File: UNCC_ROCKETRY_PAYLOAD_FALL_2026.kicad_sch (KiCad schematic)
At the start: 0 parts

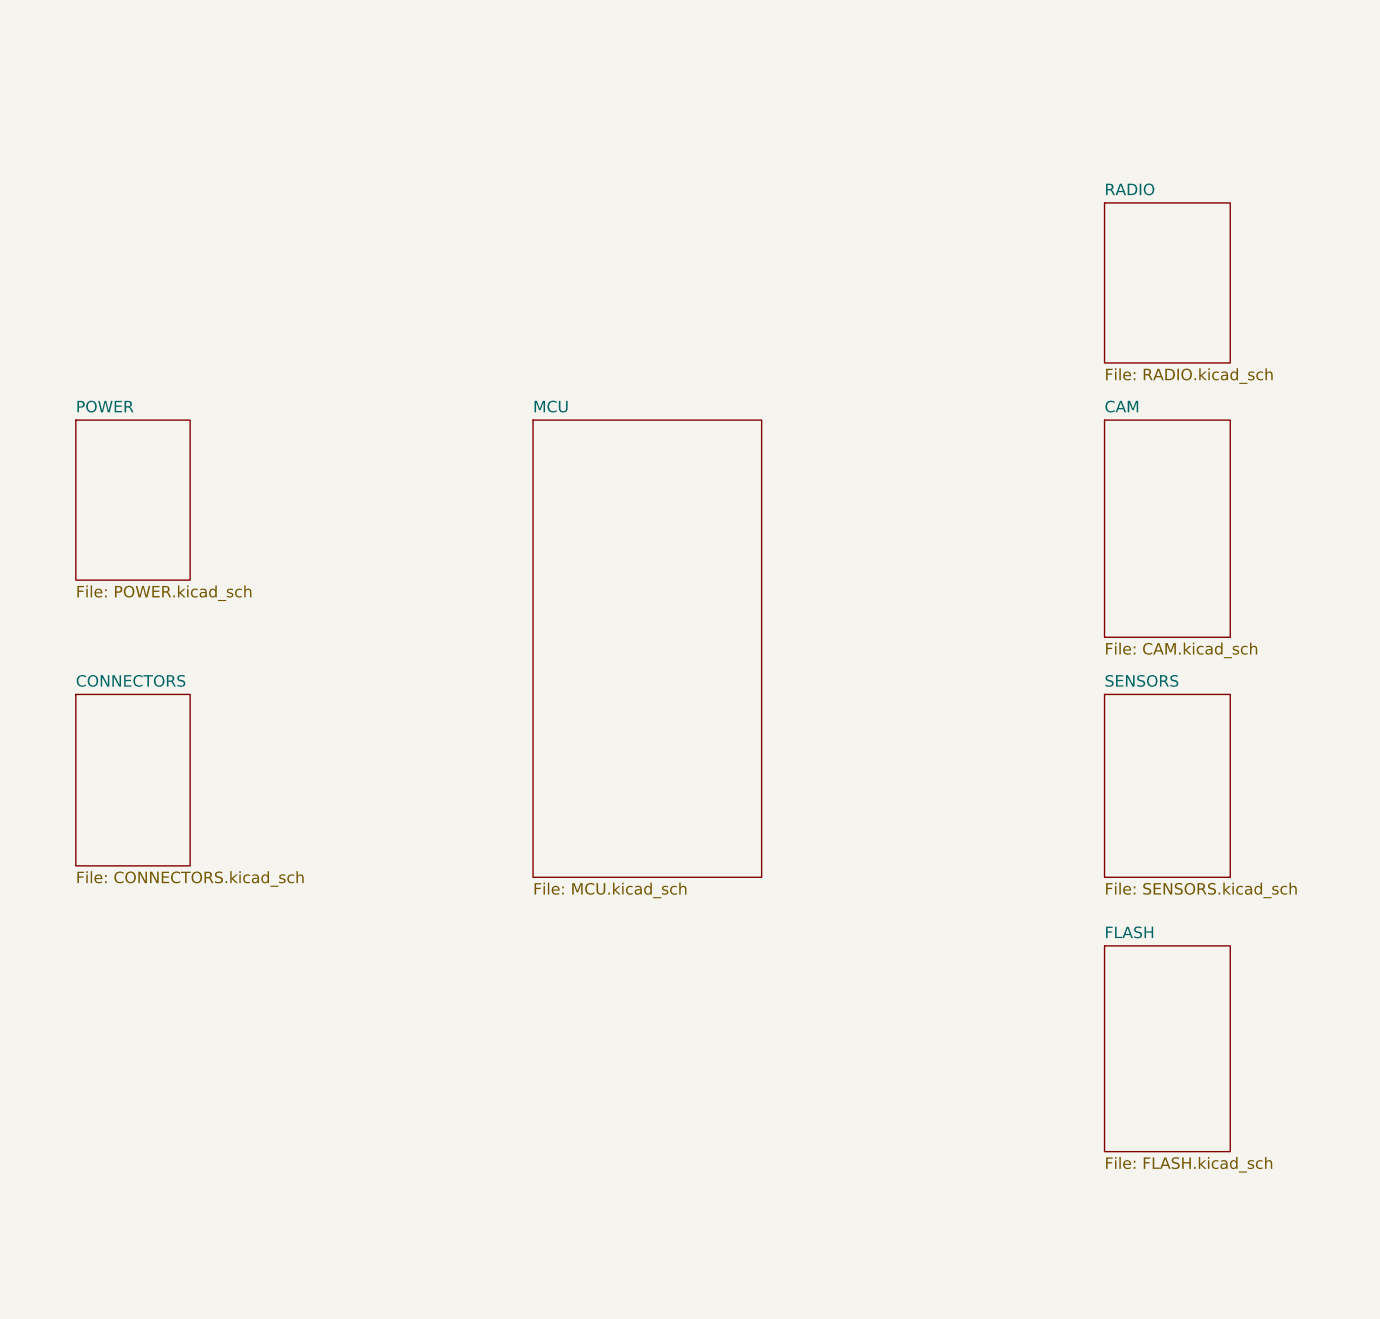
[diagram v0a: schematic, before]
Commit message: added micro and 3 sensors and connectors with USB
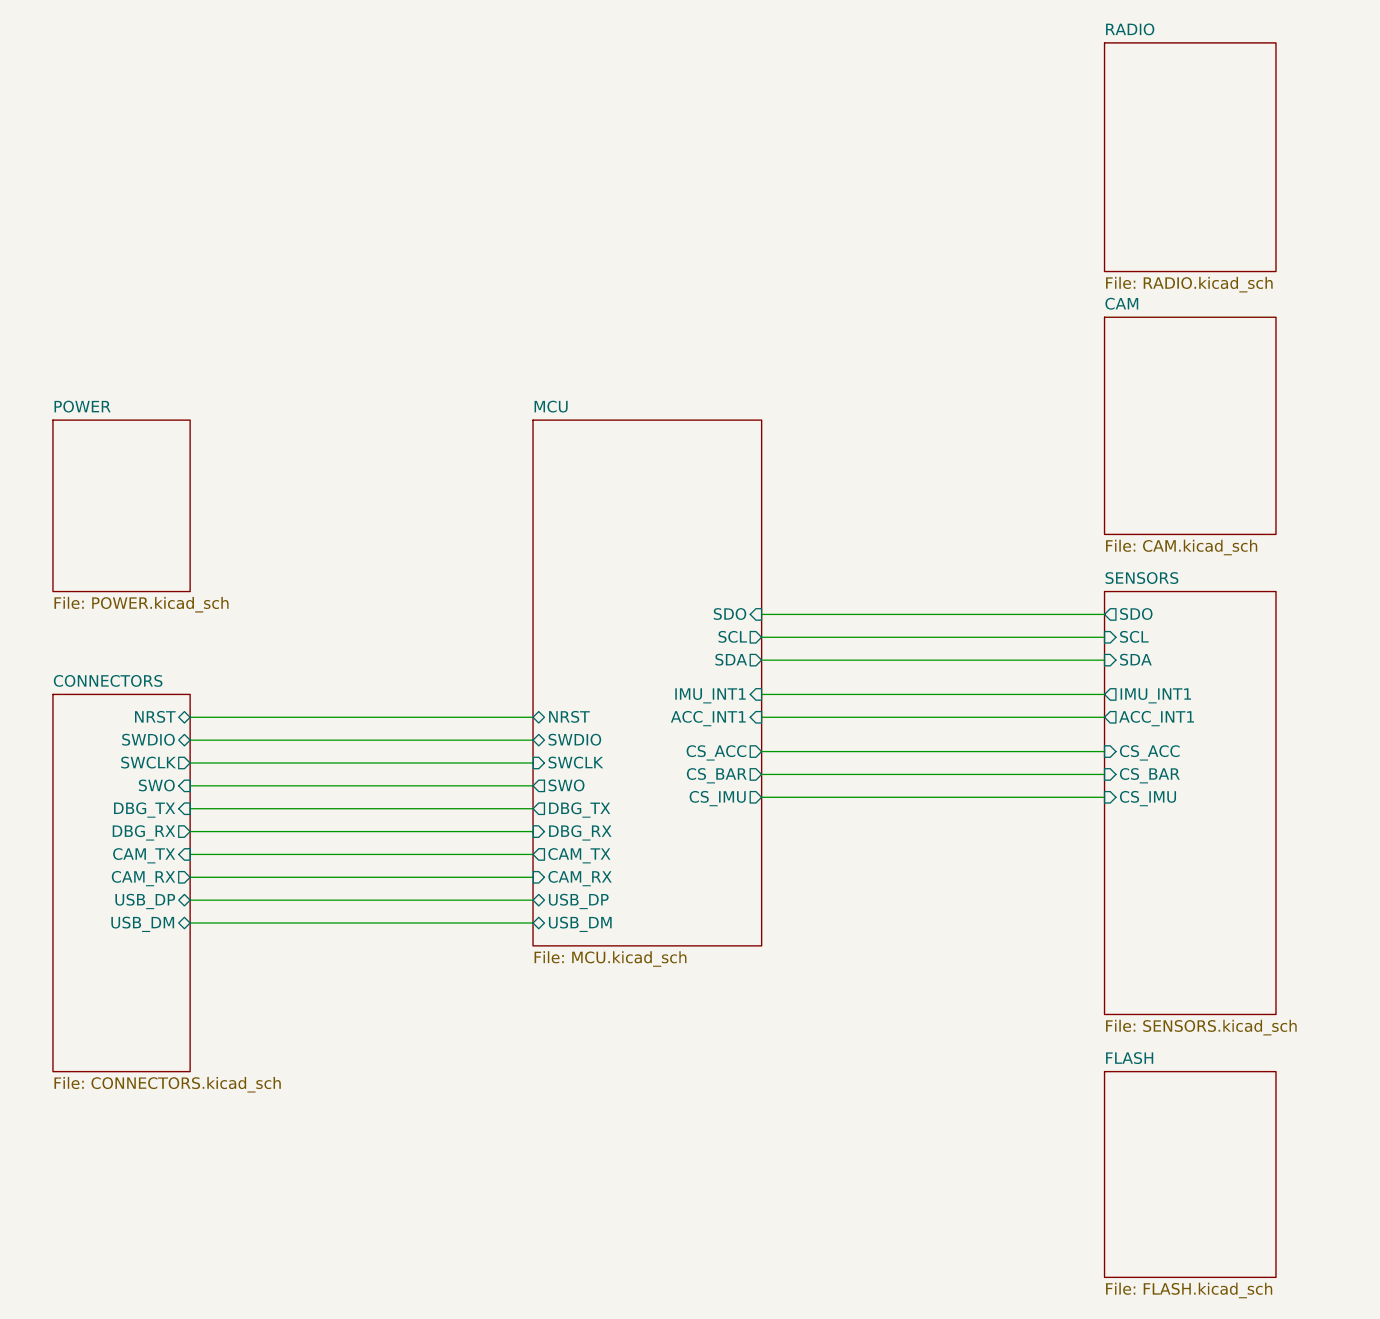
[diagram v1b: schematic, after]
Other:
- sheet CONNECTORS ports: added CAM_RX, CAM_TX, DBG_RX, DBG_TX, NRST, SWCLK, SWDIO, SWO, USB_DM, USB_DP; removed none
- sheet MCU ports: added ACC_INT1, CAM_RX, CAM_TX, CS_ACC, CS_BAR, CS_IMU, DBG_RX, DBG_TX, IMU_INT1, NRST, SCL, SDA, SDO, SWCLK, SWDIO, SWO, USB_DM, USB_DP; removed none
- sheet SENSORS ports: added ACC_INT1, CS_ACC, CS_BAR, CS_IMU, IMU_INT1, SCL, SDA, SDO; removed none

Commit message: cleaned up Schematic
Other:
- sheet RADIO renamed RF
- sheet RF: file RADIO.kicad_sch -> RF.kicad_sch

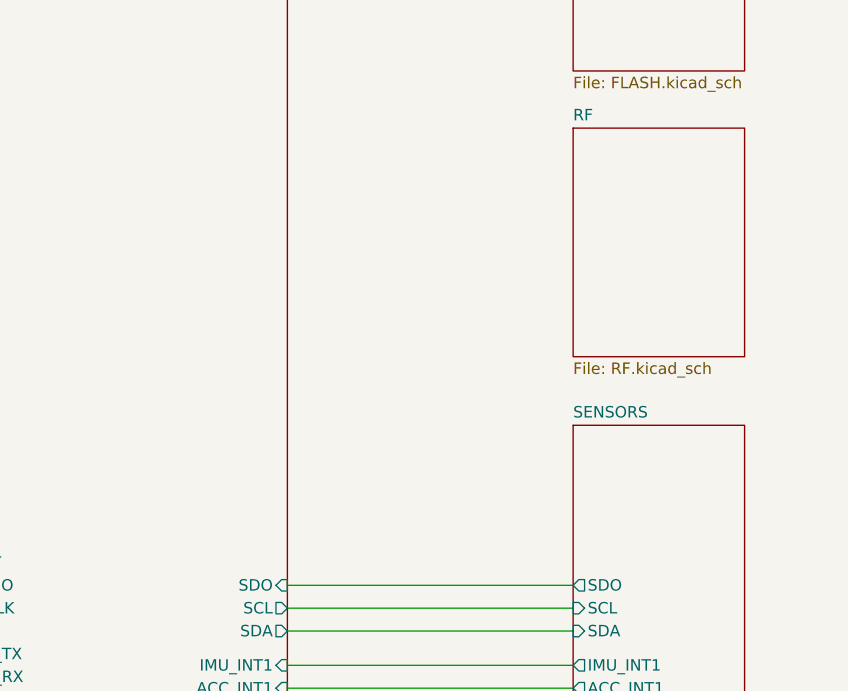
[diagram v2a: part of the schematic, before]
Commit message: added GPS and Temp/Humid sensor
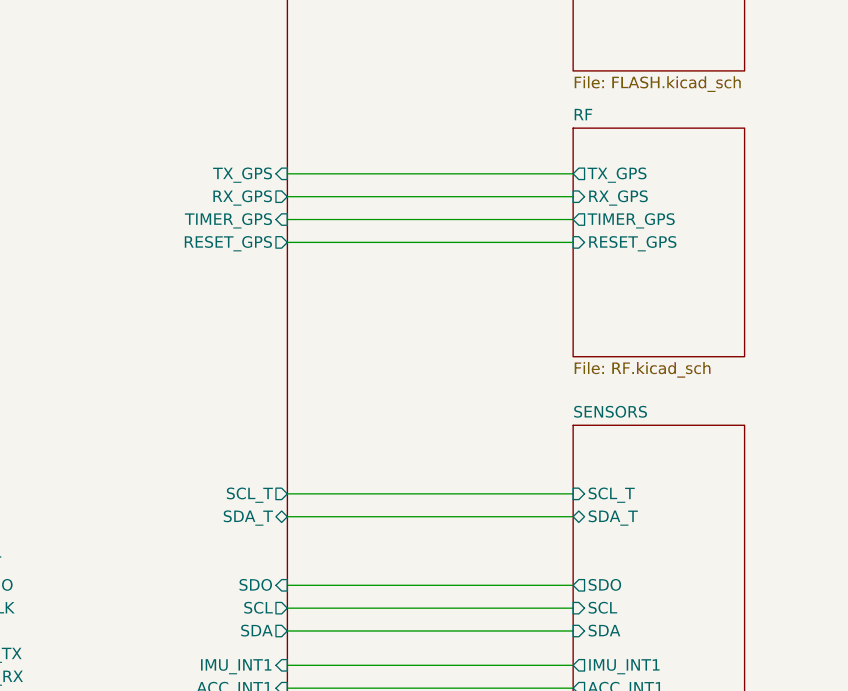
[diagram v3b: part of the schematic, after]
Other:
- sheet MCU ports: added RESET_GPS, RX_GPS, SCL_T, SDA_T, TIMER_GPS, TX_GPS; removed none
- sheet RF ports: added RESET_GPS, RX_GPS, TIMER_GPS, TX_GPS; removed none
- sheet SENSORS ports: added SCL_T, SDA_T; removed none
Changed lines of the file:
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@@
+	(wire
+		(pts
+			(xy 158.75 91.44) (xy 190.5 91.44)
+		)
+		(stroke
+			(width 0)
+			(type default)
+		)
+	)
 	(wire
 		(pts
@@
 	(wire
 		(pts
+			(xy 158.75 93.98) (xy 190.5 93.98)
+		)
+		(stroke
+			(width 0)
+			(type default)
+		)
+	)
+	(wire
+		(pts
+			(xy 158.75 86.36) (xy 190.5 86.36)
+		)
+		(stroke
+			(width 0)
+			(type default)
+		)
+	)
+	(wire
+		(pts
 			(xy 158.75 149.86) (xy 190.5 149.86)
 		)
@@
 	(wire
 		(pts
+			(xy 158.75 121.92) (xy 190.5 121.92)
+		)
+		(stroke
+			(width 0)
+			(type default)
+		)
+	)
+	(wire
+		(pts
 			(xy 88.9 144.78) (xy 120.65 144.78)
+		)
+		(stroke
+			(width 0)
+			(type default)
+		)
+	)
+	(wire
+		(pts
+			(xy 158.75 88.9) (xy 190.5 88.9)
+		)
+		(stroke
+			(width 0)
+			(type default)
+		)
+	)
+	(wire
+		(pts
+			(xy 158.75 124.46) (xy 190.5 124.46)
 		)
 		(stroke
@@
 			)
 		)
+		(pin "SCL_T" input
+			(at 190.5 121.92 180)
+			(effects
+				(font
+					(size 1.27 1.27)
+				)
+				(justify left)
+			)
+		)
+		(pin "SDA_T" bidirectional
+			(at 190.5 124.46 180)
+			(effects
+				(font
+					(size 1.27 1.27)
+				)
+				(justify left)
+			)
+		)
 		(instances
 			(project "UNCC_ROCKETRY_PAYLOAD_FALL_2026"
@@
 			)
 		)
+		(pin "TX_GPS" input
+			(at 158.75 86.36 0)
+			(effects
+				(font
+					(size 1.27 1.27)
+				)
+				(justify right)
+			)
+		)
+		(pin "RX_GPS" output
+			(at 158.75 88.9 0)
+			(effects
+				(font
+					(size 1.27 1.27)
+				)
+				(justify right)
+			)
+		)
+		(pin "TIMER_GPS" input
+			(at 158.75 91.44 0)
+			(effects
+				(font
+					(size 1.27 1.27)
+				)
+				(justify right)
+			)
+		)
+		(pin "RESET_GPS" output
+			(at 158.75 93.98 0)
+			(effects
+				(font
+					(size 1.27 1.27)
+				)
+				(justify right)
+			)
+		)
+		(pin "SCL_T" output
+			(at 158.75 121.92 0)
+			(effects
+				(font
+					(size 1.27 1.27)
+				)
+				(justify right)
+			)
+		)
+		(pin "SDA_T" bidirectional
+			(at 158.75 124.46 0)
+			(effects
+				(font
+					(size 1.27 1.27)
+				)
+				(justify right)
+			)
+		)
 		(instances
 			(project "UNCC_ROCKETRY_PAYLOAD_FALL_2026"
@@
 			)
 		)
+		(pin "TX_GPS" output
+			(at 190.5 86.36 180)
+			(effects
+				(font
+					(size 1.27 1.27)
+				)
+				(justify left)
+			)
+		)
+		(pin "RX_GPS" input
+			(at 190.5 88.9 180)
+			(effects
+				(font
+					(size 1.27 1.27)
+				)
+				(justify left)
+			)
+		)
+		(pin "TIMER_GPS" output
+			(at 190.5 91.44 180)
+			(effects
+				(font
+					(size 1.27 1.27)
+				)
+				(justify left)
+			)
+		)
+		(pin "RESET_GPS" input
+			(at 190.5 93.98 180)
+			(effects
+				(font
+					(size 1.27 1.27)
+				)
+				(justify left)
+			)
+		)

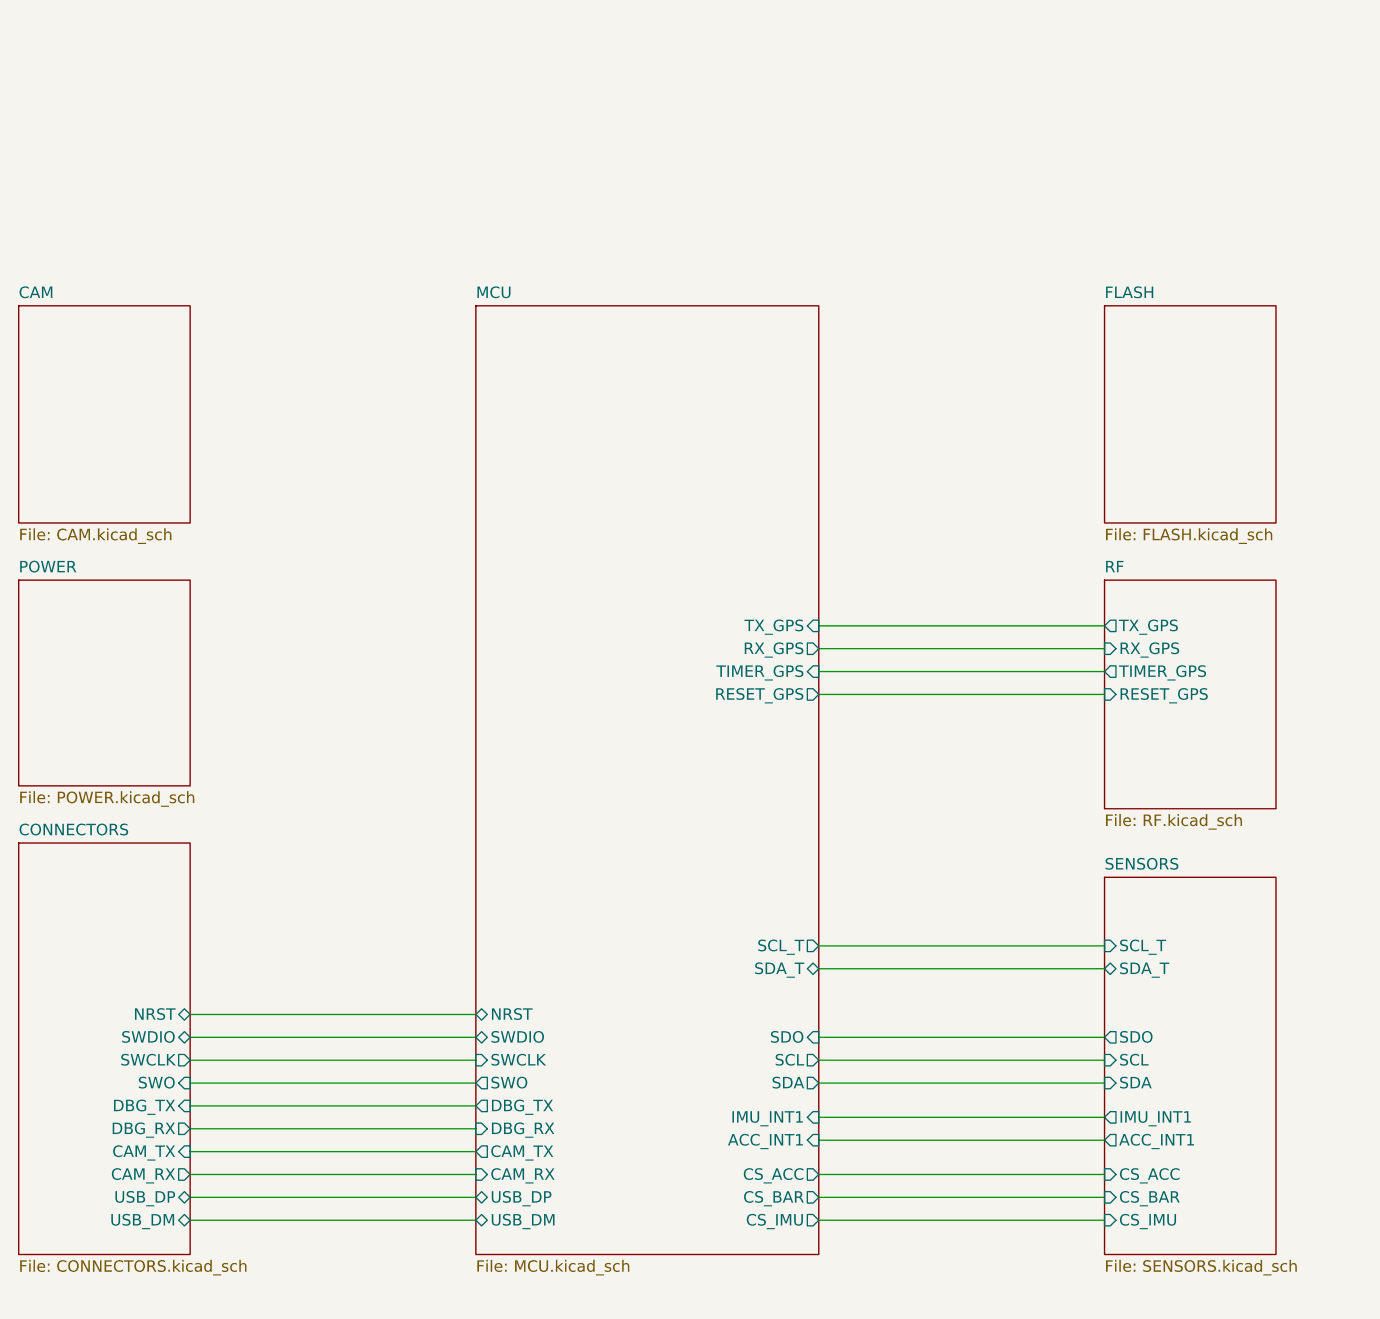
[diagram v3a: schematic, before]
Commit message: added Buzzer, status LEDs
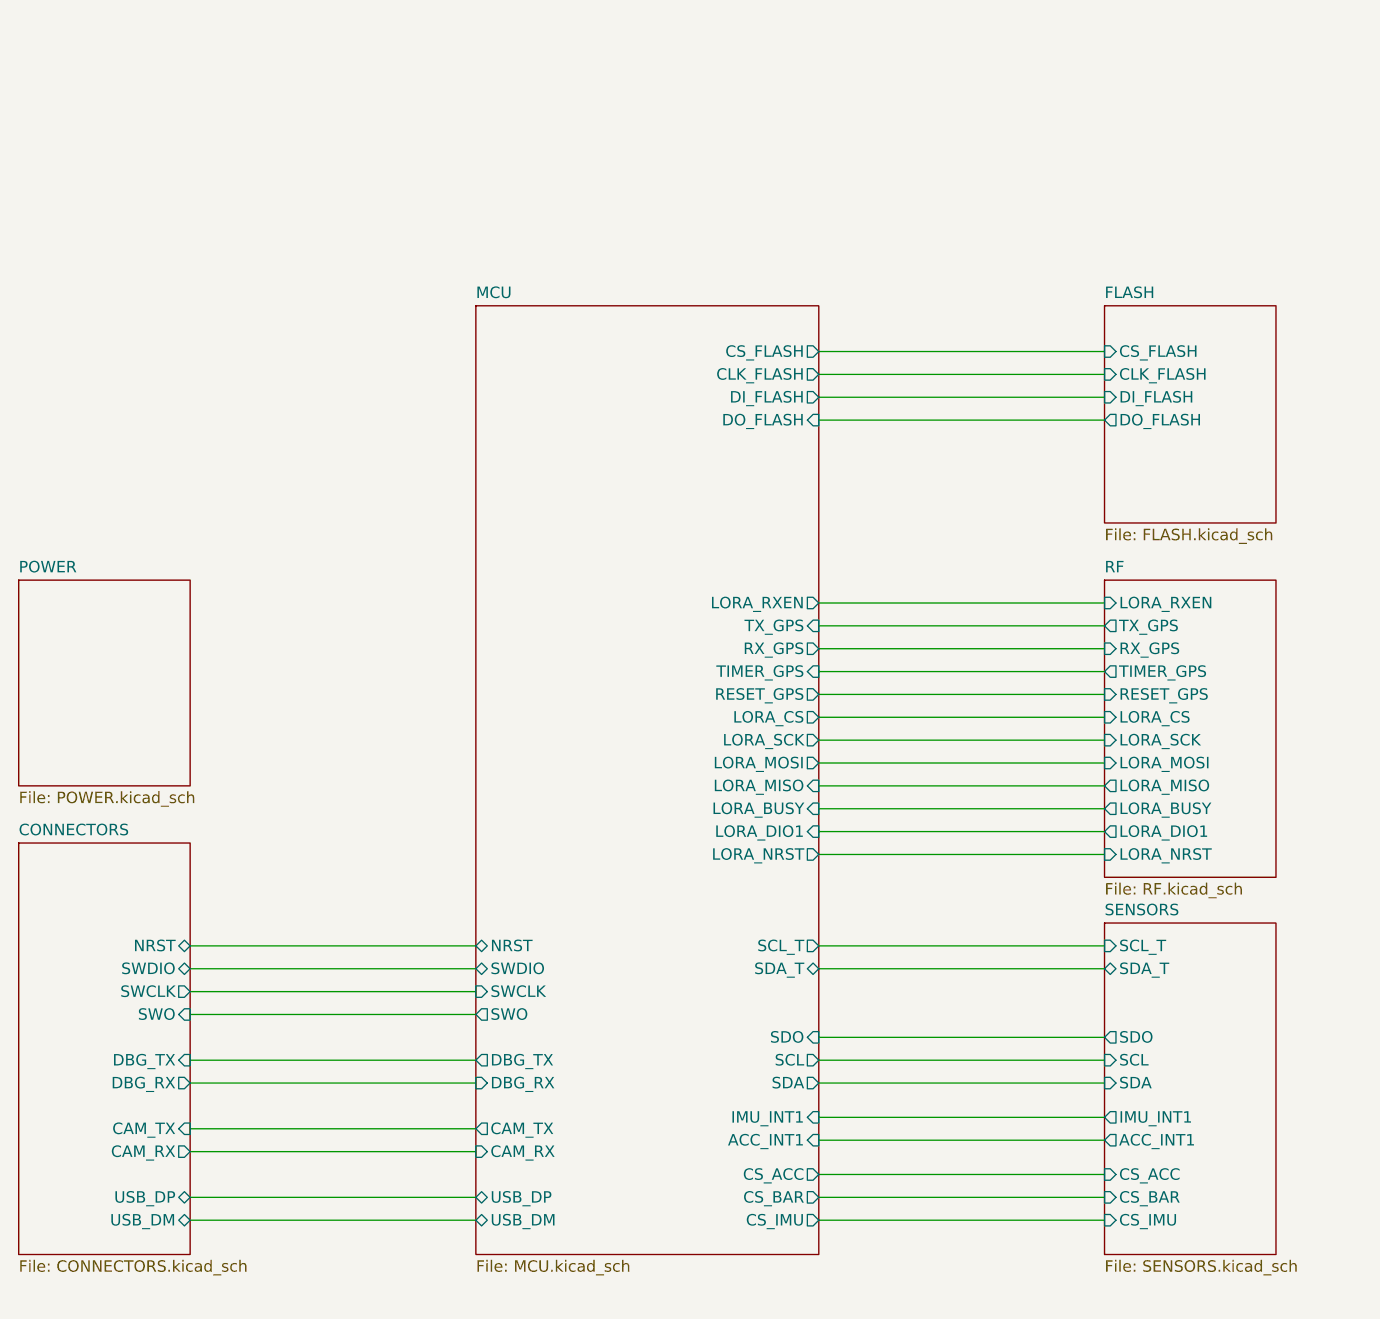
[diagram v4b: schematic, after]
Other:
- removed sheet CAM
- sheet FLASH ports: added CLK_FLASH, CS_FLASH, DI_FLASH, DO_FLASH; removed none
- sheet MCU ports: added CLK_FLASH, CS_FLASH, DI_FLASH, DO_FLASH, LORA_BUSY, LORA_CS, LORA_DIO1, LORA_MISO, LORA_MOSI, LORA_NRST, LORA_RXEN, LORA_SCK; removed none
- sheet RF ports: added LORA_BUSY, LORA_CS, LORA_DIO1, LORA_MISO, LORA_MOSI, LORA_NRST, LORA_RXEN, LORA_SCK; removed none
